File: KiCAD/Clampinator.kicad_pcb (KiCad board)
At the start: 4 copper layers, 200 x 115 mm, 204 parts, among them J1 Power, J10 Conn_01x04, J11 Conn_01x04, J12 FDCAN_1, J13 FDCAN_2, J14 10k NTC, J15 10k NTC, J16 EN_NTC_B, J17 EN_NTC_A, J18 FAN, J19 FAN, J20 VP0265840000G, J23 VP0265840000G, J24 VP0265840000G, J25 +5V INJ, J26 UART4, J5 Debug Header, J6 Conn_01x04, J7 Conn_01x04, J8 Conn_01x04, J9 Conn_01x04, Q1 TK100E10N1,S1X, Q10 AO3400A, Q2 TK100E10N1,S1X, Q3 TK100E10N1,S1X, Q4 TK100E10N1,S1X, Q5 TK100E10N1,S1X, Q6 TK100E10N1,S1X, Q9 MMBT3904-C20526, SW1 PTS810SJM250SMTRLFS, SW2 PTS810SJM250SMTRLFS, SW3 PTS810SJM250SMTRLFS, SW4 PTS810SJM250SMTRLFS, SW5 SMQS-02R-TP, SW6 EG1847-ND, SW7 GPI-154-3013, U1 STM32H573RIT6, U10 LM74810QDRRRQ1, U12 TPS7A2033DQNR, U13 VOS618A-3T, U14 LM5163DDAR, U2 TL432BQDBZR, U3 EG2131, U4 UCC33420RAQR_C46461551, U5 USBLC6-2SC6, U6 LM5012DDAR, U7 MCP2562FD-E/P, U8 MCP2562FD-E/P, U9 EL357N, X1 SC-32S32.768kHz20PPM7pF, Y2 ECS-80-18-23B-JTM-TR

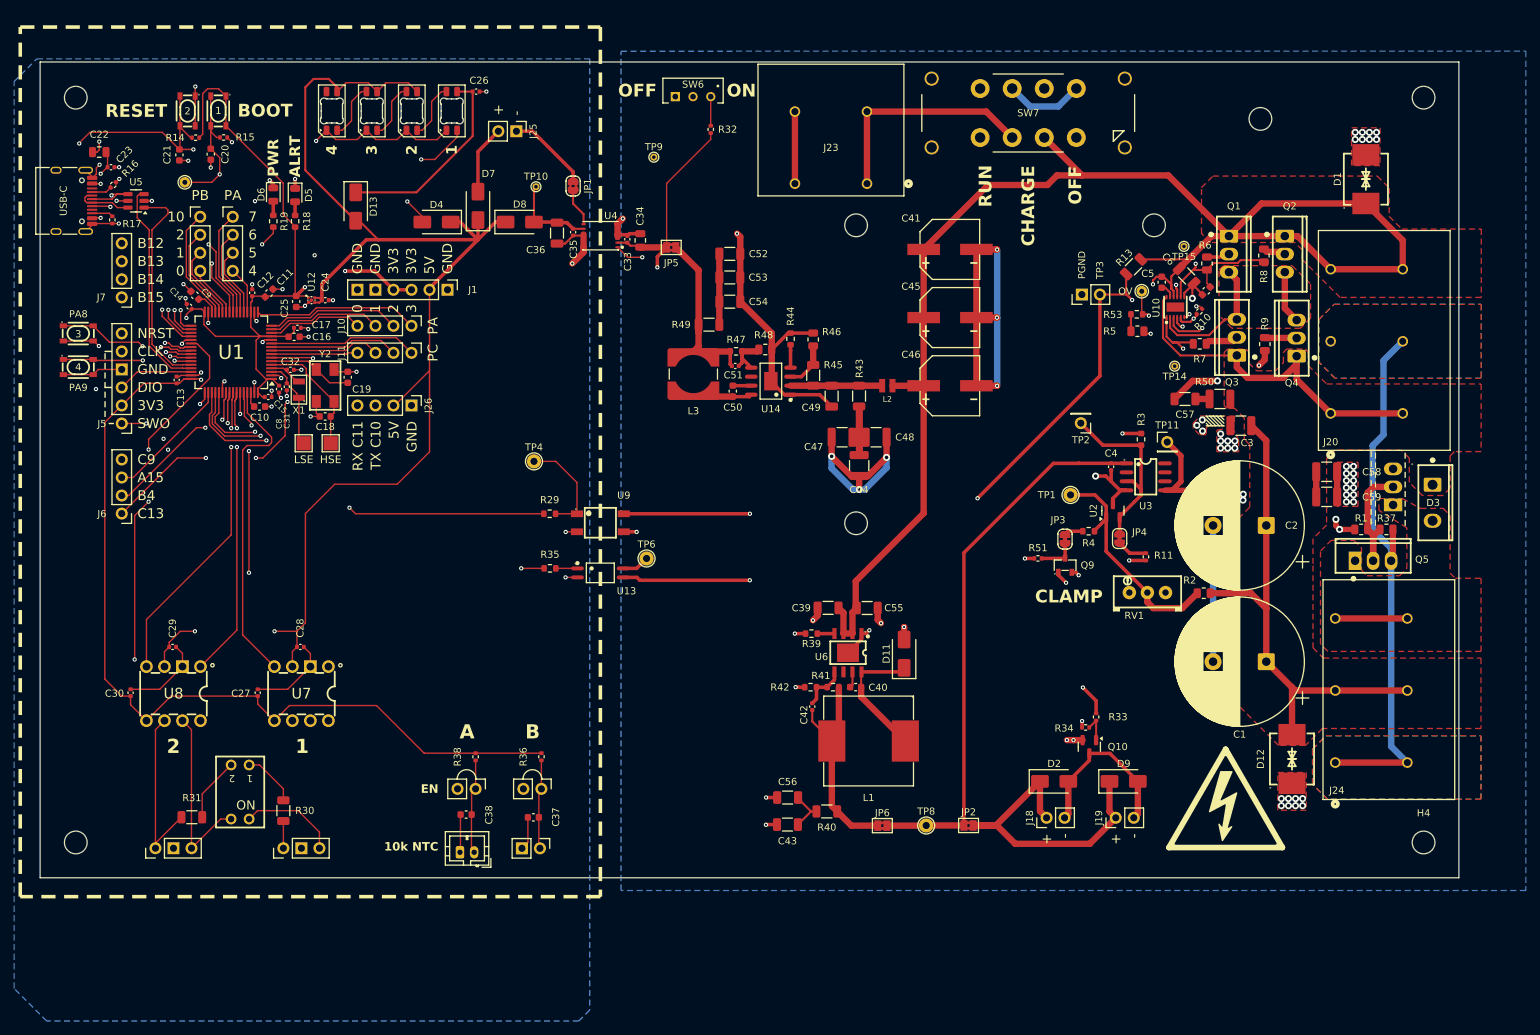
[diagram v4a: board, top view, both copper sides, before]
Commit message: Fixed footprint libraries, corrected terminal block footprints, added 3d model for precharge resistor terminal block
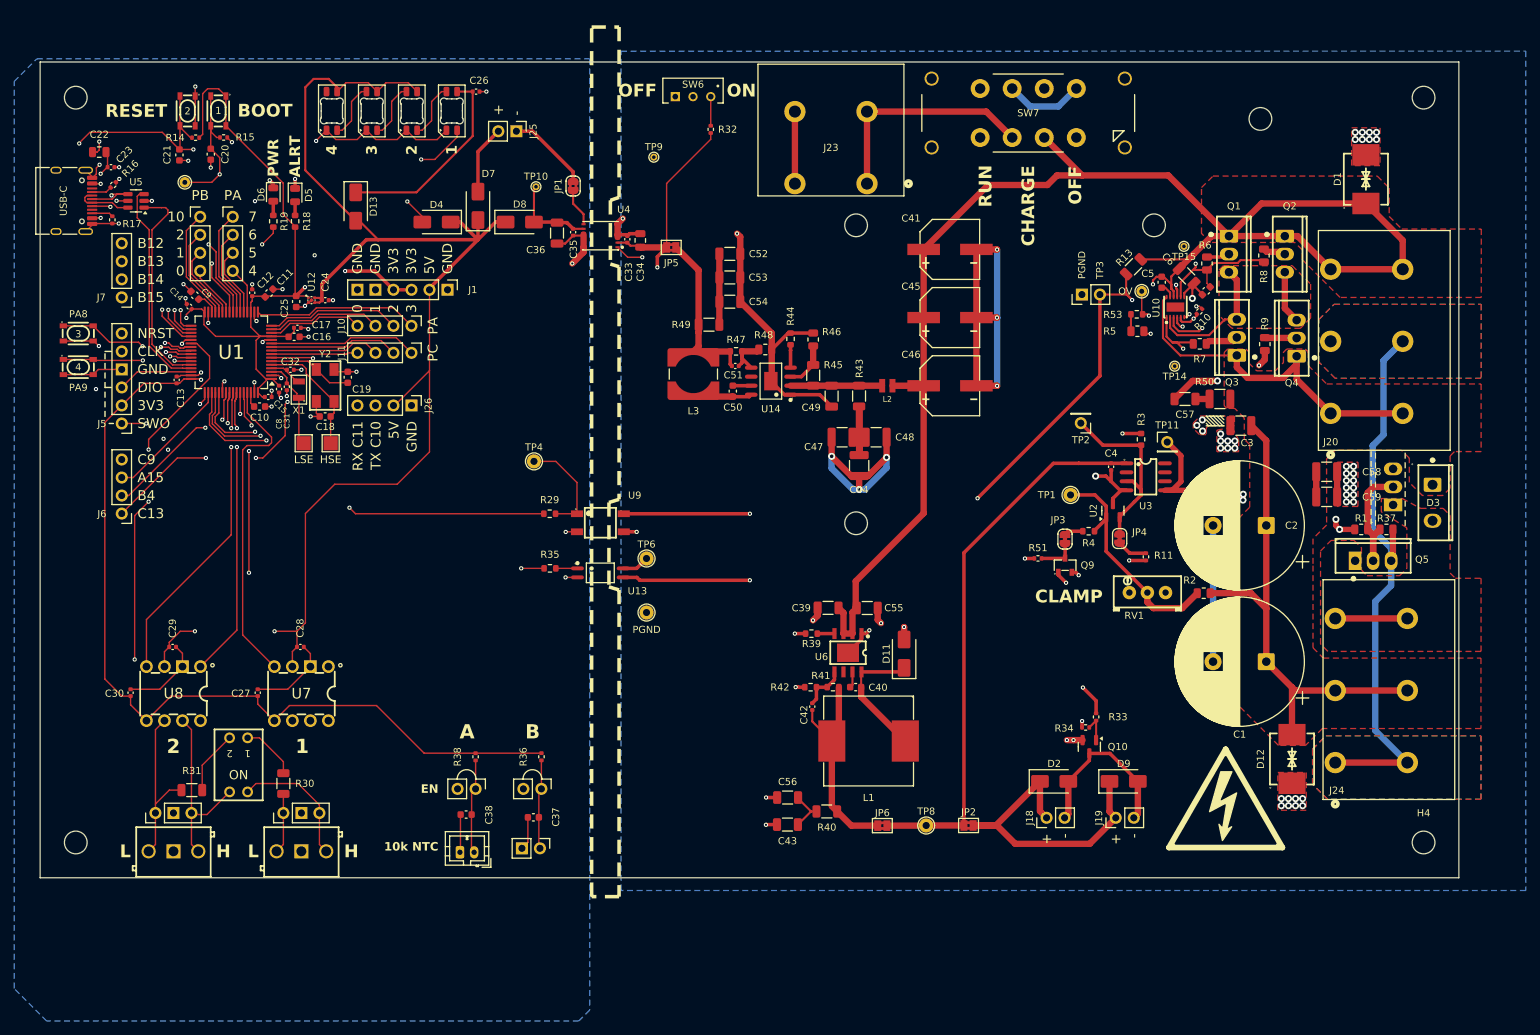
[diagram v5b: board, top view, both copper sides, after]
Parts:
- added J27: Screw_Terminal_01x03, easyeda2kicad:CONN-TH_3P-P3.50_OSTTE030161, F.Cu at (84.6, 135.8)
- added J28: Screw_Terminal_01x03, easyeda2kicad:CONN-TH_3P-P3.50_OSTTE030161, F.Cu at (66.6, 135.8)
- added TP16: PGND, TestPoint:TestPoint_THTPad_D2.0mm_Drill1.0mm, F.Cu at (133.3, 102.1)
- J20, J24: value VP0265840000G -> VP0365840000G
- moved J12 4.96 mm to (82.1, 130.4)
- moved J13 4.96 mm to (64.1, 130.4)
- moved SW5 3.83 mm to (75.8, 123.6)
- moved R30 3.82 mm to (82.1, 126.2)
- moved R31 3.82 mm to (69.2, 127.2)
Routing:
- net DC_GND: track 293.3 -> 295.1 mm
- net CANL_2: track 24.4 -> 23.8 mm
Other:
- board text added: "H"
- board text added: "L"
